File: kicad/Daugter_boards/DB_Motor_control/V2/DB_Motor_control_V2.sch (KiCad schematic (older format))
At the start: 8 parts, among them P1 CONN_01X19, P2 CONN_01X15, P3 CONN_01X15, P4 CONN_01X08, P5 CONN_01X08, P6 CONN_01X04, P7 CONN_01X19

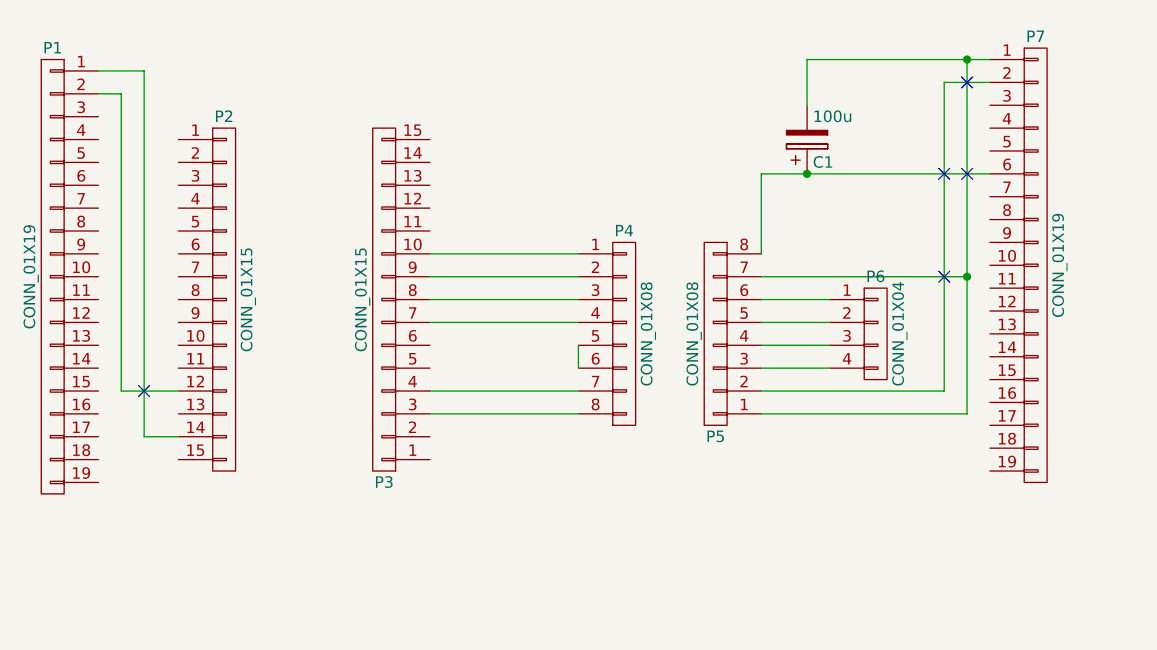
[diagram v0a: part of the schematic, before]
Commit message: adding DB_Motor_Control
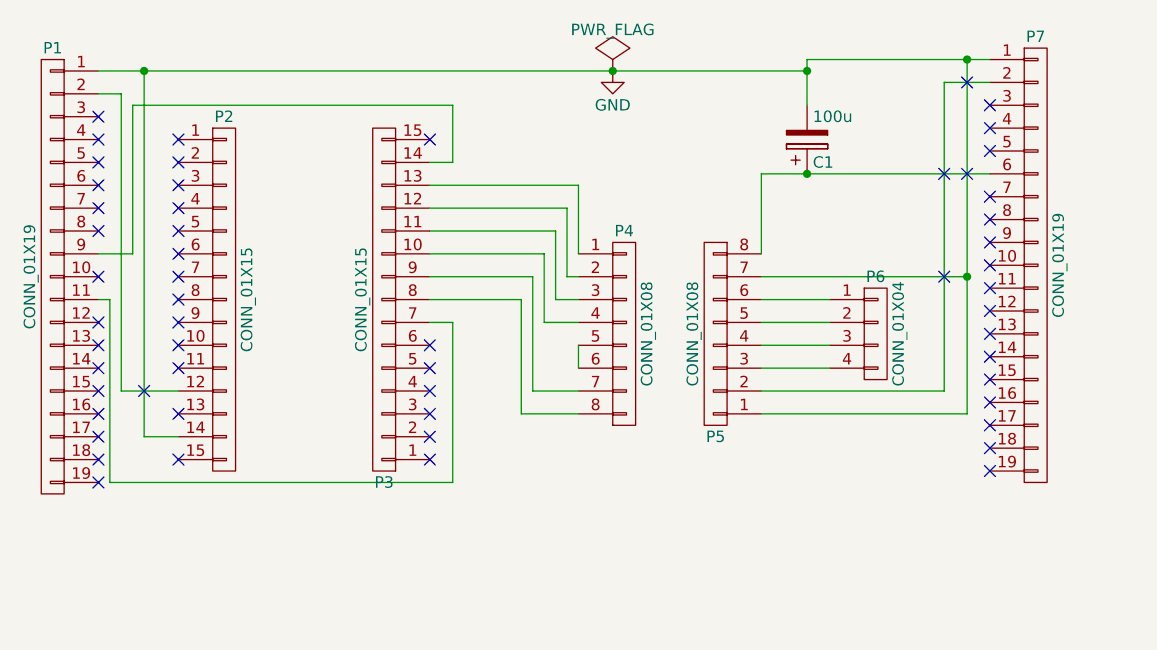
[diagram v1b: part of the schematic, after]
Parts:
- C1: footprint (none) -> Capacitors_ThroughHole:C_Radial_D5_L6_P2.5
- P1, P7: footprint (none) -> Socket_Strips:Socket_Strip_Straight_1x19
- P2, P3: footprint (none) -> Socket_Strips:Socket_Strip_Straight_1x15
- P4, P5: footprint (none) -> Socket_Strips:Socket_Strip_Straight_1x08
- P6: footprint (none) -> Socket_Strips:Socket_Strip_Straight_1x04
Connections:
- net at P4.1 (P1): now also P3.13 (P13); no longer P3.10 (P10)
- net at P4.2 (P2): now also P3.12 (P12); no longer P3.9 (P9)
- net at P4.3 (P3): now also P3.11 (P11); no longer P3.8 (P8)
- net at P4.4 (P4): now also P3.10 (P10); no longer P3.7 (P7)
- net at P4.7 (P7): now also P3.9 (P9); no longer P3.4 (P4)
- net at P4.8 (P8): now also P3.8 (P8); no longer P3.3 (P3)
- net GND: now reaches C1.2, P5.1 (P1), P5.7 (P7), P7.1 (P1)
- net GND: now also P1.1 (P1), P2.14 (P14)
- net at P3.14 (P14): now also P1.9 (P9)
- net at P1.11 (P11): now also P3.7 (P7)
- no-connect marks 5 -> 56
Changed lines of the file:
@@
 LIBS:valves
 LIBS:echopen
+LIBS:DB_Motor_control_V2-cache
 EELAYER 25 0
 EELAYER END
@@
 F 0 "P6" H 6650 4300 50  0000 C CNN
 F 1 "CONN_01X04" V 6750 4050 50  0000 C CNN
-F 2 "" H 6650 4050 50  0000 C CNN
+F 2 "Socket_Strips:Socket_Strip_Straight_1x04" H 6650 4050 50  0001 C CNN
 F 3 "" H 6650 4050 50  0000 C CNN
 	1    6650 4050
@@
 F 0 "P4" H 5550 4500 50  0000 C CNN
 F 1 "CONN_01X08" V 5650 4050 50  0000 C CNN
-F 2 "" H 5550 4050 50  0000 C CNN
+F 2 "Socket_Strips:Socket_Strip_Straight_1x08" H 5550 4050 50  0001 C CNN
 F 3 "" H 5550 4050 50  0000 C CNN
 	1    5550 4050
@@
 F 0 "P5" H 5950 4500 50  0000 C CNN
 F 1 "CONN_01X08" V 6050 4050 50  0000 C CNN
-F 2 "" H 5950 4050 50  0000 C CNN
+F 2 "Socket_Strips:Socket_Strip_Straight_1x08" H 5950 4050 50  0001 C CNN
 F 3 "" H 5950 4050 50  0000 C CNN
 	1    5950 4050
@@
 F 0 "P2" H 3800 4700 50  0000 C CNN
 F 1 "CONN_01X15" V 3900 3900 50  0000 C CNN
-F 2 "" H 3800 3900 50  0000 C CNN
+F 2 "Socket_Strips:Socket_Strip_Straight_1x15" H 3800 3900 50  0001 C CNN
 F 3 "" H 3800 3900 50  0000 C CNN
 	1    3800 3900
@@
 F 0 "P3" H 4500 4700 50  0000 C CNN
 F 1 "CONN_01X15" V 4600 3900 50  0000 C CNN
-F 2 "" H 4500 3900 50  0000 C CNN
+F 2 "Socket_Strips:Socket_Strip_Straight_1x15" H 4500 3900 50  0001 C CNN
 F 3 "" H 4500 3900 50  0000 C CNN
 	1    4500 3900
@@
 F 0 "P7" H 7350 4750 50  0000 C CNN
 F 1 "CONN_01X19" V 7450 3750 50  0000 C CNN
-F 2 "" H 7350 3750 50  0000 C CNN
+F 2 "Socket_Strips:Socket_Strip_Straight_1x19" H 7350 3750 50  0001 C CNN
 F 3 "" H 7350 3750 50  0000 C CNN
 	1    7350 3750
@@
 F 0 "P1" H 3050 4800 50  0000 C CNN
 F 1 "CONN_01X19" V 3150 3800 50  0000 C CNN
-F 2 "" H 3050 3800 50  0000 C CNN
+F 2 "Socket_Strips:Socket_Strip_Straight_1x19" H 3050 3800 50  0001 C CNN
 F 3 "" H 3050 3800 50  0000 C CNN
 	1    3050 3800
@@
 F 0 "C1" H 6375 3300 50  0000 L CNN
 F 1 "100u" H 6375 3100 50  0000 L CNN
-F 2 "" H 6388 3050 50  0000 C CNN
+F 2 "Capacitors_ThroughHole:C_Radial_D5_L6_P2.5" H 6388 3050 50  0001 C CNN
 F 3 "" H 6350 3200 50  0000 C CNN
 	1    6350 3200
@@
 	5350 4100 5350 4200
 Wire Wire Line
-	5350 4400 4700 4400
-Wire Wire Line
-	5350 4300 4700 4300
-Wire Wire Line
-	5350 4000 4700 4000
-Wire Wire Line
-	5350 3900 4700 3900
-Wire Wire Line
-	5350 3800 4700 3800
-Wire Wire Line
-	5350 3700 4700 3700
-Wire Wire Line
 	6450 3900 6150 3900
 Wire Wire Line
@@
 	3450 4500 3450 2900
 Wire Wire Line
-	3450 2900 3250 2900
+	3250 2900 6350 2900
 Wire Wire Line
 	6150 4300 6950 4300
@@
 	6950 2950 7150 2950
 Wire Wire Line
-	6150 4400 7050 4400
-Wire Wire Line
-	7050 4400 7050 2850
+	7050 4400 6150 4400
+Wire Wire Line
+	7050 2850 7050 4400
 Wire Wire Line
 	6350 2850 7150 2850
 Wire Wire Line
-	7150 3350 6150 3350
+	6150 3350 7150 3350
 Wire Wire Line
 	6150 3350 6150 3700
@@
 Connection ~ 7050 2850
 Connection ~ 6350 3350
+Connection ~ 6350 2900
+Connection ~ 3450 2900
+NoConn ~ 3250 3100
+NoConn ~ 3250 3200
+NoConn ~ 3250 3300
+NoConn ~ 3250 3400
+NoConn ~ 3250 3500
+NoConn ~ 3250 3600
+NoConn ~ 3250 3800
+NoConn ~ 3250 4000
+NoConn ~ 3250 4100
+NoConn ~ 3250 4200
+NoConn ~ 3250 4300
+NoConn ~ 3250 4400
+NoConn ~ 3250 4500
+NoConn ~ 3250 4600
+NoConn ~ 3250 4700
+NoConn ~ 3600 4600
+NoConn ~ 3600 4400
+NoConn ~ 3600 4200
+NoConn ~ 3600 4100
+NoConn ~ 3600 4000
+NoConn ~ 3600 3900
+NoConn ~ 3600 3800
+NoConn ~ 3600 3700
+NoConn ~ 3600 3600
+NoConn ~ 3600 3500
+NoConn ~ 3600 3400
+NoConn ~ 3600 3300
+NoConn ~ 3600 3200
+NoConn ~ 4700 3200
+NoConn ~ 4700 4500
+NoConn ~ 4700 4600
+NoConn ~ 7150 4650
+NoConn ~ 7150 4550
+NoConn ~ 7150 4450
+NoConn ~ 7150 4350
+NoConn ~ 7150 4250
+NoConn ~ 7150 4150
+NoConn ~ 7150 4050
+NoConn ~ 7150 3950
+NoConn ~ 7150 3850
+NoConn ~ 7150 3750
+NoConn ~ 7150 3650
+NoConn ~ 7150 3550
+NoConn ~ 7150 3450
+NoConn ~ 7150 3250
+NoConn ~ 7150 3150
+NoConn ~ 7150 3050
+Wire Wire Line
+	4700 3400 5350 3400
+Wire Wire Line
+	5350 3400 5350 3700
+Wire Wire Line
+	4700 3500 5300 3500
+Wire Wire Line
+	5300 3500 5300 3800
+Wire Wire Line
+	5300 3800 5350 3800
+Wire Wire Line
+	4700 3600 5250 3600
+Wire Wire Line
+	5250 3600 5250 3900
+Wire Wire Line
+	5250 3900 5350 3900
+Wire Wire Line
+	4700 3700 5200 3700
+Wire Wire Line
+	5200 3700 5200 4000
+Wire Wire Line
+	5200 4000 5350 4000
+Wire Wire Line
+	4700 3800 5150 3800
+Wire Wire Line
+	5150 3800 5150 4300
+Wire Wire Line
+	5150 4300 5350 4300
+Wire Wire Line
+	4700 3900 5100 3900
+Wire Wire Line
+	5100 3900 5100 4400
+Wire Wire Line
+	5100 4400 5350 4400
+Wire Wire Line
+	3250 3700 3400 3700
+Wire Wire Line
+	3400 3700 3400 3050
+Wire Wire Line
+	3400 3050 4800 3050
+Wire Wire Line
+	4800 3050 4800 3300
+Wire Wire Line
+	4800 3300 4700 3300
+$Comp
+L PWR_FLAG #FLG01
+U 1 1 57B326EE
+P 5500 2900
+F 0 "#FLG01" H 5500 2995 50  0001 C CNN
+F 1 "PWR_FLAG" H 5500 3080 50  0000 C CNN
+F 2 "" H 5500 2900 50  0000 C CNN
+F 3 "" H 5500 2900 50  0000 C CNN
+	1    5500 2900
+	1    0    0    -1
+$EndComp
+$Comp
+L GND #PWR02
+U 1 1 57B3271A
+P 5500 2900
+F 0 "#PWR02" H 5500 2650 50  0001 C CNN
+F 1 "GND" H 5500 2750 50  0000 C CNN
+F 2 "" H 5500 2900 50  0000 C CNN
+F 3 "" H 5500 2900 50  0000 C CNN
+	1    5500 2900
+	1    0    0    -1
+$EndComp
+Connection ~ 5500 2900
+NoConn ~ 4700 4100
+NoConn ~ 4700 4200
+NoConn ~ 4700 4300
+NoConn ~ 4700 4400
+Wire Wire Line
+	3250 3900 3300 3900
+Wire Wire Line
+	3300 3900 3300 4700
+Wire Wire Line
+	3300 4700 4800 4700
+Wire Wire Line
+	4800 4700 4800 4000
+Wire Wire Line
+	4800 4000 4700 4000
 $EndSCHEMATC
